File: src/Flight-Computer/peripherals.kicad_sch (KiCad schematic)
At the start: 32 parts, among them P10 Micro_SD_Card, P3 USB, P4 282837-6, Q1 QS5U17TR, Q2 QS5U17TR, U10 RFM95W-868S2, U3 CP2102-GMR(QFN28), U4 SST25VF040B-50-4I-S2AE-T, U5 TS391IYLT, U6 TS391IYLT, U7 TS391IYLT

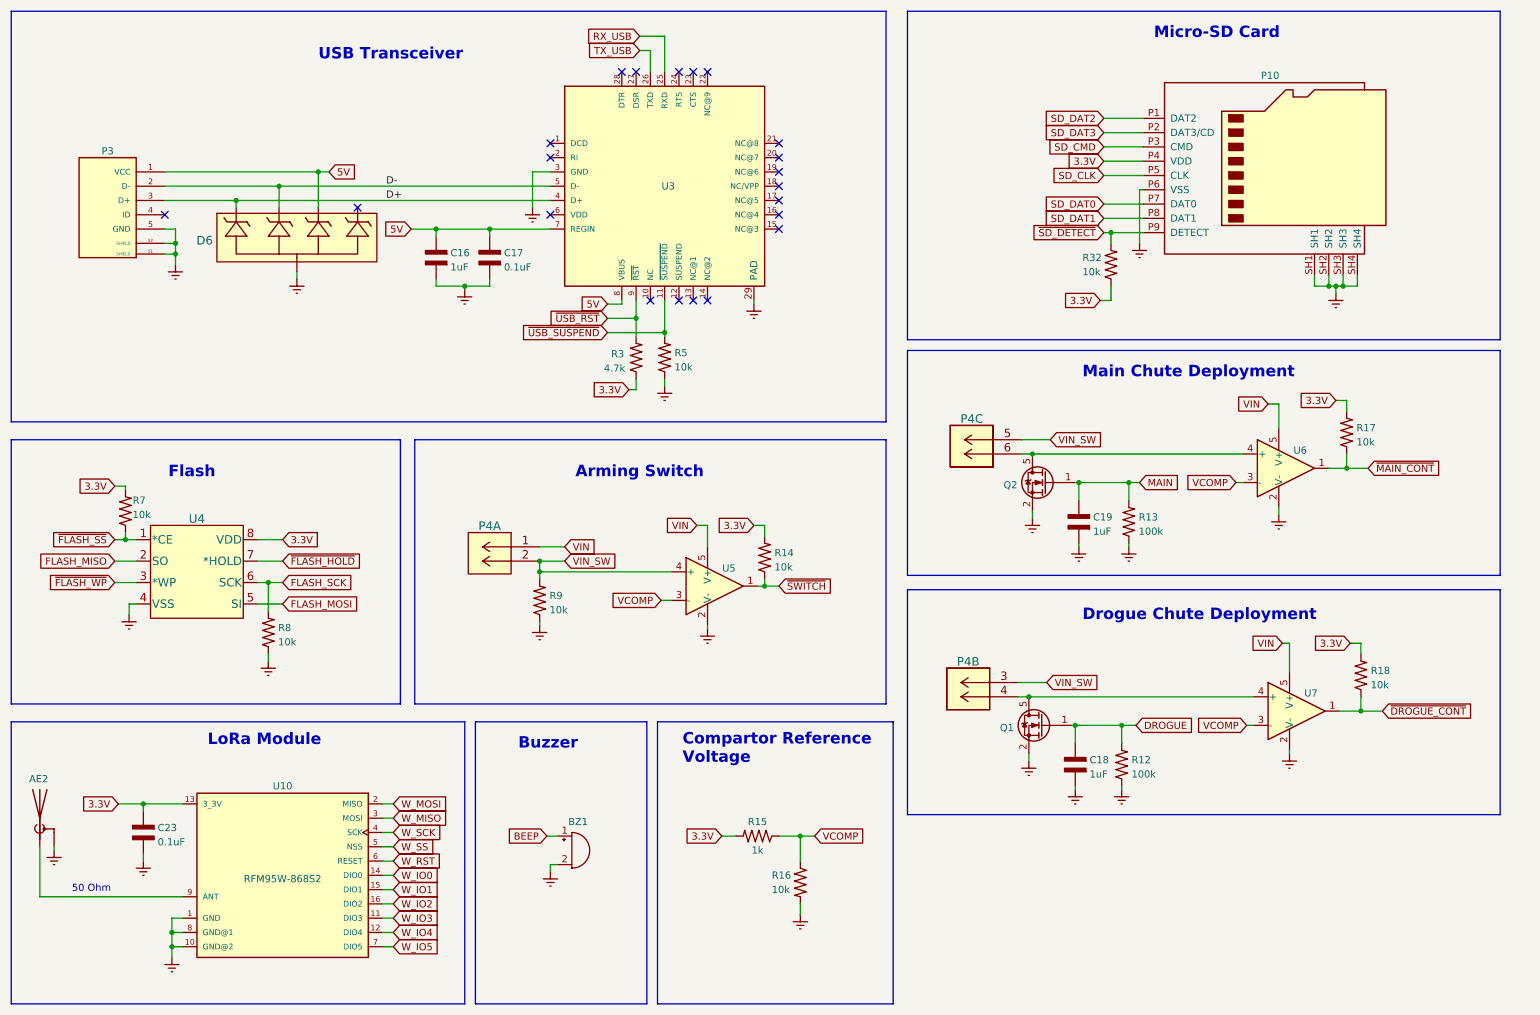
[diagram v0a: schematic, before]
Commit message: added usb detector to schemtaic
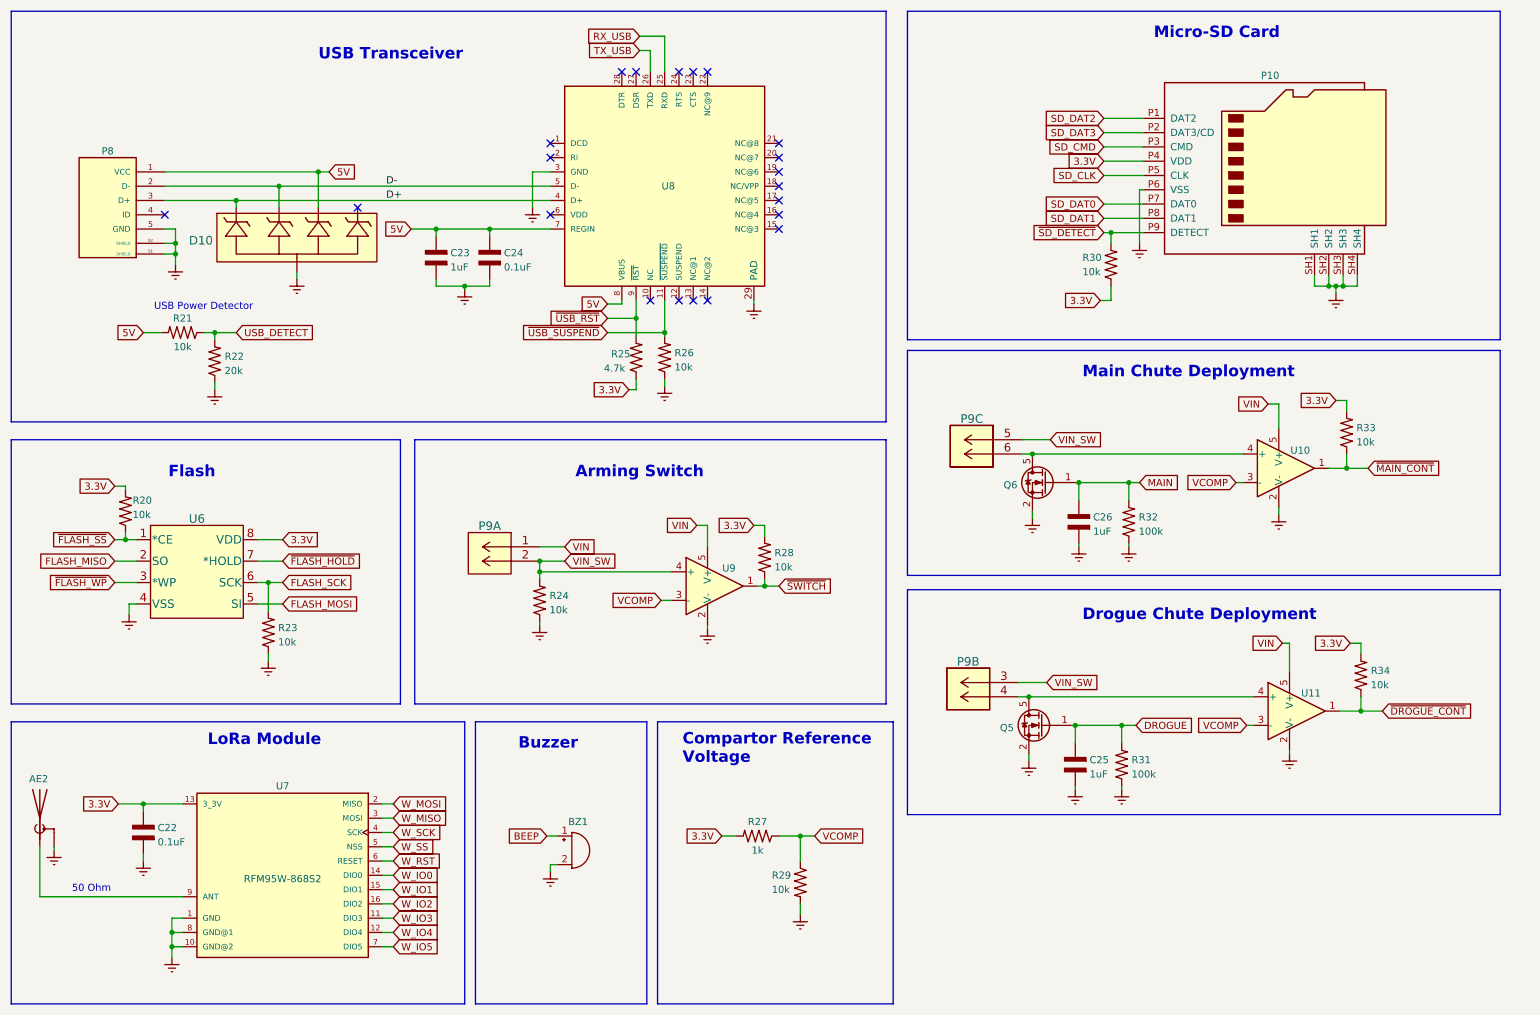
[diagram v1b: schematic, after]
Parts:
- added R21: 10k, Flight-Computer:RES_0603, symbol Flight-Computer:RES_0603
- added R22: 20k, Flight-Computer:RES_0603, symbol Flight-Computer:RES_0603
- renumbered C23 to C22, C16 to C23, C17 to C24, C18 to C25, C19 to C26, D6 to D10, P3 to P8, P4 to P9, Q1 to Q5, Q2 to Q6, R7 to R20, R8 to R23, R9 to R24, R3 to R25, R5 to R26, R15 to R27, R14 to R28, R16 to R29, R32 to R30, R12 to R31, R13 to R32, R17 to R33, R18 to R34, U6 to U10, U7 to U11, U4 to U6, U10 to U7, U3 to U8, U5 to U9
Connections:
- net 5V: now also R21.2
- net Earth: now also R22.1
- new net USB_DETECT: R21.1, R22.2
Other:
- note added: "USB Power Detector"

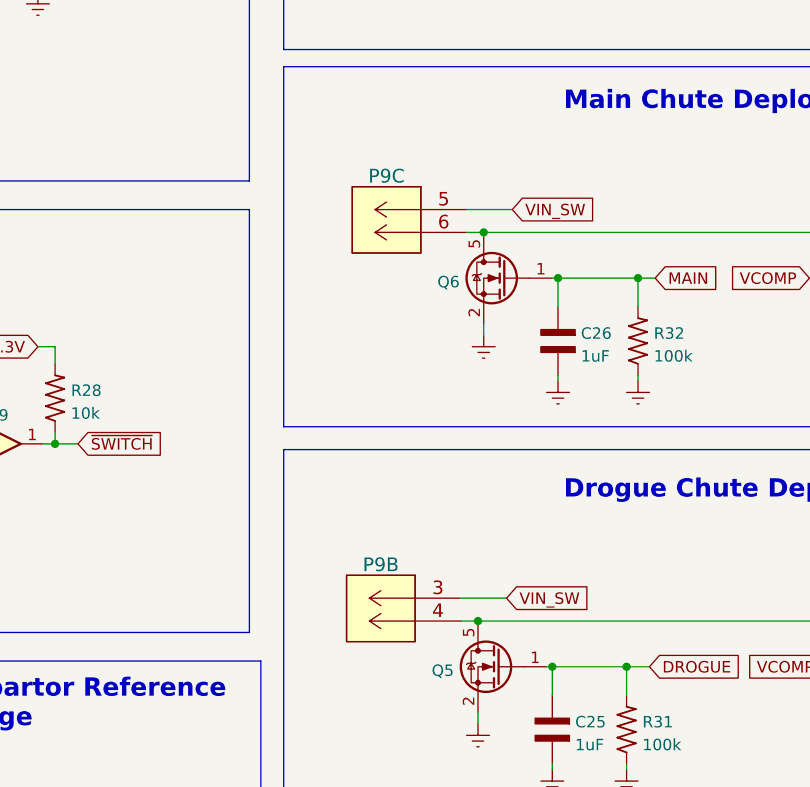
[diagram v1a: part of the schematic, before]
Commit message: replaced screw terminals with smaller parts
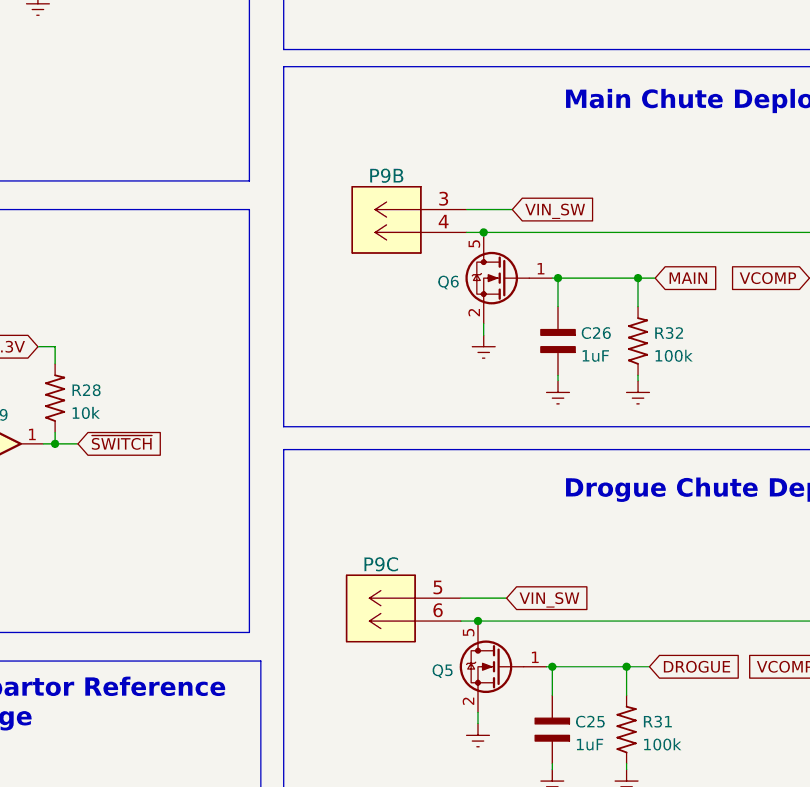
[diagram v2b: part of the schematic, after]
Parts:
- removed P9: 282837-6, Flight-Computer:282837-6, symbol Flight-Computer:282837-6
- added P9: 1984659, Flight-Computer:1984659, symbol Flight-Computer:1984659
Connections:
- net VIN: now also P9.1 (5)
- net VIN_SW: now also P9.2 (6), P9.3 (5), P9.5
- net at Q5.5 (D), U11.4 (+): now also P9.6
- net at Q6.5 (D), U10.4 (+): now also P9.4 (6)
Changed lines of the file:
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@@
   (junction (at 257.81 142.875) (diameter 0) (color 0 0 0 0)
   )
+  (junction (at 111.76 116.205) (diameter 0) (color 0 0 0 0)
+  )
   (junction (at 63.5 120.015) (diameter 0) (color 0 0 0 0)
   )
@@
   )
   (junction (at 41.275 159.385) (diameter 0) (color 0 0 0 0)
-  )
-  (junction (at 111.76 116.205) (diameter 0) (color 0 0 0 0)
   )
   (junction (at 254.635 67.31) (diameter 0) (color 0 0 0 0)
@@
     (pin "9")
   )
-  (symbol (lib_id "Flight-Computer:282837-6") (at 111.76 113.665 0) (mirror y) (unit 1)
-    (in_bom yes) (on_board yes) (fields_autoplaced)
-    (property "Reference" "P9" (id 0) (at 102.87 109.9581 0)
+  (symbol (lib_id "Flight-Computer:QS5U17TR") (at 201.295 145.415 0) (mirror y) (unit 1)
+    (in_bom yes) (on_board yes)
+    (property "Reference" "Q5" (id 0) (at 196.088 145.8488 0)
+      (effects (font (size 1.27 1.27)) (justify left))
+    )
+    (property "Value" "QS5U17TR" (id 1) (at 198.12 158.115 0)
+      (effects (font (size 1.27 1.27)) (justify left) hide)
+    )
+    (property "Footprint" "Engine-Controller:QS5U17TR" (id 2) (at 199.39 161.29 0)
+      (effects (font (size 1.27 1.27) italic) (justify left) hide)
+    )
+    (property "Datasheet" "https://www.onsemi.com/pub/Collateral/NDS7002A-D.PDF" (id 3) (at 202.565 164.465 0)
+      (effects (font (size 1.27 1.27)) (justify left) hide)
+    )
+    (pin "1")
+    (pin "2")
+    (pin "3")
+    (pin "4")
+    (pin "5")
+  )
+  (symbol (lib_id "Flight-Computer:1984659") (at 197.485 94.615 0) (mirror y) (unit 2)
+    (in_bom yes) (on_board yes) (fields_autoplaced)
+    (property "Reference" "P9" (id 0) (at 188.595 90.9081 0)
       (effects (font (size 1.524 1.524)))
     )
-    (property "Value" "282837-6" (id 1) (at 106.68 141.605 0)
+    (property "Value" "1984659" (id 1) (at 192.405 122.555 0)
       (effects (font (size 1.524 1.524)) hide)
     )
-    (property "Footprint" "Flight-Computer:282837-6" (id 2) (at 107.95 144.145 0)
+    (property "Footprint" "Flight-Computer:1984659" (id 2) (at 193.675 125.095 0)
       (effects (font (size 1.524 1.524)) hide)
     )
-    (property "Datasheet" "" (id 3) (at 111.76 113.665 0)
+    (property "Datasheet" "" (id 3) (at 197.485 94.615 0)
       (effects (font (size 1.524 1.524)) hide)
     )
@@
     (pin "5")
     (pin "6")
-  )
-  (symbol (lib_id "Flight-Computer:QS5U17TR") (at 201.295 145.415 0) (mirror y) (unit 1)
-    (in_bom yes) (on_board yes)
-    (property "Reference" "Q5" (id 0) (at 196.088 145.8488 0)
-      (effects (font (size 1.27 1.27)) (justify left))
-    )
-    (property "Value" "QS5U17TR" (id 1) (at 198.12 158.115 0)
-      (effects (font (size 1.27 1.27)) (justify left) hide)
-    )
-    (property "Footprint" "Engine-Controller:QS5U17TR" (id 2) (at 199.39 161.29 0)
-      (effects (font (size 1.27 1.27) italic) (justify left) hide)
-    )
-    (property "Datasheet" "https://www.onsemi.com/pub/Collateral/NDS7002A-D.PDF" (id 3) (at 202.565 164.465 0)
-      (effects (font (size 1.27 1.27)) (justify left) hide)
-    )
-    (pin "1")
-    (pin "2")
-    (pin "3")
-    (pin "4")
-    (pin "5")
   )
   (symbol (lib_id "Flight-Computer:TS391IYLT") (at 244.475 99.695 0) (unit 1)
@@
     (pin "2")
   )
-  (symbol (lib_id "Flight-Computer:Earth") (at 158.115 179.07 0) (unit 1)
-    (in_bom yes) (on_board yes) (fields_autoplaced)
-    (property "Reference" "#PWR050" (id 0) (at 158.115 185.42 0)
-      (effects (font (size 1.27 1.27)) hide)
-    )
-    (property "Value" "Earth" (id 1) (at 158.115 182.88 0)
-      (effects (font (size 1.27 1.27)) hide)
-    )
-    (property "Footprint" "" (id 2) (at 158.115 179.07 0)
-      (effects (font (size 1.27 1.27)) hide)
-    )
-    (property "Datasheet" "" (id 3) (at 158.115 179.07 0)
-      (effects (font (size 1.27 1.27)) hide)
-    )
-    (pin "1")
-  )
-  (symbol (lib_name "RES_0603_7") (lib_id "Flight-Computer:RES_0603") (at 255.27 93.345 90) (unit 1)
-    (in_bom yes) (on_board yes) (fields_autoplaced)
-    (property "Reference" "R33" (id 0) (at 257.0226 92.5103 90)
-      (effects (font (size 1.27 1.27)) (justify right))
-    )
-    (property "Value" "10k" (id 1) (at 257.0226 95.0472 90)
-      (effects (font (size 1.27 1.27)) (justify right))
-    )
-    (property "Footprint" "Flight-Computer:RES_0603" (id 2) (at 267.97 92.075 0)
-      (effects (font (size 1.27 1.27)) (justify left bottom) hide)
-    )
-    (property "Datasheet" "" (id 3) (at 255.27 93.345 0)
-      (effects (font (size 1.27 1.27)) (justify left bottom) hide)
-    )
-    (pin "1")
-    (pin "2")
-  )
-  (symbol (lib_id "Flight-Computer:Earth") (at 46.99 63.5 0) (unit 1)
-    (in_bom yes) (on_board yes) (fields_autoplaced)
-    (property "Reference" "#PWR039" (id 0) (at 46.99 69.85 0)
-      (effects (font (size 1.27 1.27)) hide)
-    )
-    (property "Value" "Earth" (id 1) (at 46.99 67.31 0)
-      (effects (font (size 1.27 1.27)) hide)
-    )
-    (property "Footprint" "" (id 2) (at 46.99 63.5 0)
-      (effects (font (size 1.27 1.27)) hide)
-    )
-    (property "Datasheet" "" (id 3) (at 46.99 63.5 0)
-      (effects (font (size 1.27 1.27)) hide)
-    )
-    (pin "1")
-  )
-  (symbol (lib_id "Flight-Computer:282837-6") (at 196.85 137.795 0) (mirror y) (unit 2)
+  (symbol (lib_id "Flight-Computer:1984659") (at 196.85 137.795 0) (mirror y) (unit 3)
     (in_bom yes) (on_board yes) (fields_autoplaced)
     (property "Reference" "P9" (id 0) (at 187.96 134.0881 0)
       (effects (font (size 1.524 1.524)))
     )
-    (property "Value" "282837-6" (id 1) (at 191.77 165.735 0)
+    (property "Value" "1984659" (id 1) (at 191.77 165.735 0)
       (effects (font (size 1.524 1.524)) hide)
     )
-    (property "Footprint" "Flight-Computer:282837-6" (id 2) (at 193.04 168.275 0)
+    (property "Footprint" "Flight-Computer:1984659" (id 2) (at 193.04 168.275 0)
       (effects (font (size 1.524 1.524)) hide)
     )
@@
     (pin "5")
     (pin "6")
+  )
+  (symbol (lib_id "Flight-Computer:Earth") (at 158.115 179.07 0) (unit 1)
+    (in_bom yes) (on_board yes) (fields_autoplaced)
+    (property "Reference" "#PWR050" (id 0) (at 158.115 185.42 0)
+      (effects (font (size 1.27 1.27)) hide)
+    )
+    (property "Value" "Earth" (id 1) (at 158.115 182.88 0)
+      (effects (font (size 1.27 1.27)) hide)
+    )
+    (property "Footprint" "" (id 2) (at 158.115 179.07 0)
+      (effects (font (size 1.27 1.27)) hide)
+    )
+    (property "Datasheet" "" (id 3) (at 158.115 179.07 0)
+      (effects (font (size 1.27 1.27)) hide)
+    )
+    (pin "1")
+  )
+  (symbol (lib_name "RES_0603_7") (lib_id "Flight-Computer:RES_0603") (at 255.27 93.345 90) (unit 1)
+    (in_bom yes) (on_board yes) (fields_autoplaced)
+    (property "Reference" "R33" (id 0) (at 257.0226 92.5103 90)
+      (effects (font (size 1.27 1.27)) (justify right))
+    )
+    (property "Value" "10k" (id 1) (at 257.0226 95.0472 90)
+      (effects (font (size 1.27 1.27)) (justify right))
+    )
+    (property "Footprint" "Flight-Computer:RES_0603" (id 2) (at 267.97 92.075 0)
+      (effects (font (size 1.27 1.27)) (justify left bottom) hide)
+    )
+    (property "Datasheet" "" (id 3) (at 255.27 93.345 0)
+      (effects (font (size 1.27 1.27)) (justify left bottom) hide)
+    )
+    (pin "1")
+    (pin "2")
+  )
+  (symbol (lib_id "Flight-Computer:Earth") (at 46.99 63.5 0) (unit 1)
+    (in_bom yes) (on_board yes) (fields_autoplaced)
+    (property "Reference" "#PWR039" (id 0) (at 46.99 69.85 0)
+      (effects (font (size 1.27 1.27)) hide)
+    )
+    (property "Value" "Earth" (id 1) (at 46.99 67.31 0)
+      (effects (font (size 1.27 1.27)) hide)
+    )
+    (property "Footprint" "" (id 2) (at 46.99 63.5 0)
+      (effects (font (size 1.27 1.27)) hide)
+    )
+    (property "Datasheet" "" (id 3) (at 46.99 63.5 0)
+      (effects (font (size 1.27 1.27)) hide)
+    )
+    (pin "1")
   )
   (symbol (lib_id "Flight-Computer:Micro_SD_Card") (at 241.935 45.085 0) (unit 1)
@@
     )
     (pin "1")
+  )
+  (symbol (lib_id "Flight-Computer:1984659") (at 111.76 113.665 0) (mirror y) (unit 1)
+    (in_bom yes) (on_board yes) (fields_autoplaced)
+    (property "Reference" "P9" (id 0) (at 102.87 109.9581 0)
+      (effects (font (size 1.524 1.524)))
+    )
+    (property "Value" "1984659" (id 1) (at 106.68 141.605 0)
+      (effects (font (size 1.524 1.524)) hide)
+    )
+    (property "Footprint" "Flight-Computer:1984659" (id 2) (at 107.95 144.145 0)
+      (effects (font (size 1.524 1.524)) hide)
+    )
+    (property "Datasheet" "" (id 3) (at 111.76 113.665 0)
+      (effects (font (size 1.524 1.524)) hide)
+    )
+    (pin "1")
+    (pin "2")
+    (pin "3")
+    (pin "4")
+    (pin "5")
+    (pin "6")
   )
   (symbol (lib_id "Flight-Computer:Earth") (at 199.39 108.585 0) (unit 1)
@@
     (pin "1")
   )
-  (symbol (lib_id "Flight-Computer:282837-6") (at 197.485 94.615 0) (mirror y) (unit 3)
-    (in_bom yes) (on_board yes) (fields_autoplaced)
-    (property "Reference" "P9" (id 0) (at 188.595 90.9081 0)
-      (effects (font (size 1.524 1.524)))
-    )
-    (property "Value" "282837-6" (id 1) (at 192.405 122.555 0)
-      (effects (font (size 1.524 1.524)) hide)
-    )
-    (property "Footprint" "Flight-Computer:282837-6" (id 2) (at 193.675 125.095 0)
-      (effects (font (size 1.524 1.524)) hide)
-    )
-    (property "Datasheet" "" (id 3) (at 197.485 94.615 0)
-      (effects (font (size 1.524 1.524)) hide)
-    )
-    (pin "1")
-    (pin "2")
-    (pin "3")
-    (pin "4")
-    (pin "5")
-    (pin "6")
-  )
   (symbol (lib_id "Flight-Computer:RES_0603") (at 213.36 63.5 90) (unit 1)

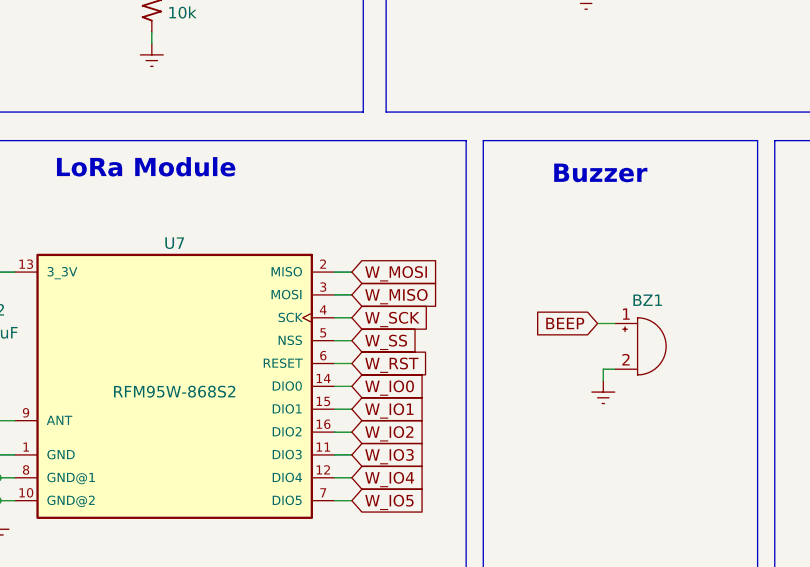
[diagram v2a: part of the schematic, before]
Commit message: fixed incorrect LoRa MISO and MOSI connections
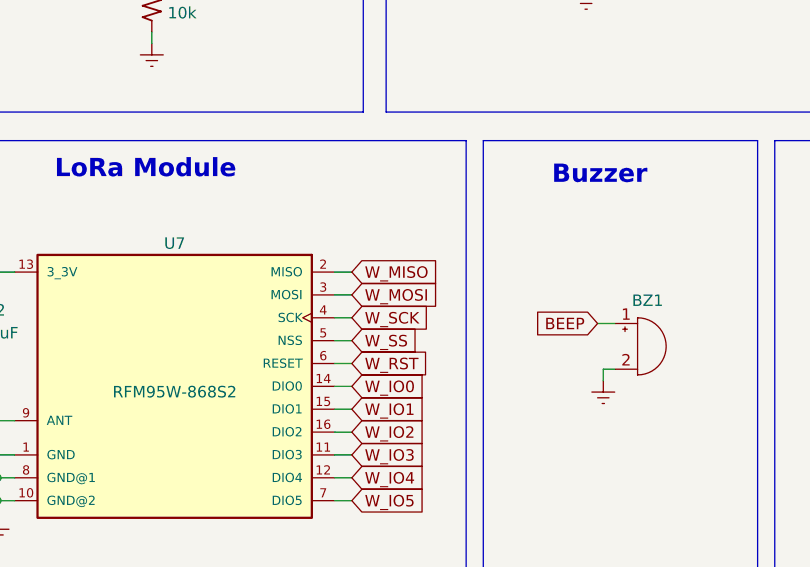
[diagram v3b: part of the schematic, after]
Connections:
- net W_MISO: now also U7.2 (MISO); no longer U7.3 (MOSI)
- net W_MOSI: now also U7.3 (MOSI); no longer U7.2 (MISO)

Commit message: matched footprints to symbols
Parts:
- Q5, Q6: footprint Engine-Controller:QS5U17TR -> Flight-Computer:QS5U17TR
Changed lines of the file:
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@@
       (effects (font (size 1.27 1.27)) (justify left) hide)
     )
-    (property "Footprint" "Engine-Controller:QS5U17TR" (id 2) (at 199.39 161.29 0)
+    (property "Footprint" "Flight-Computer:QS5U17TR" (id 2) (at 199.39 161.29 0)
       (effects (font (size 1.27 1.27) italic) (justify left) hide)
     )
@@
       (effects (font (size 1.27 1.27)) (justify left) hide)
     )
-    (property "Footprint" "Engine-Controller:QS5U17TR" (id 2) (at 200.025 118.11 0)
+    (property "Footprint" "Flight-Computer:QS5U17TR" (id 2) (at 200.025 118.11 0)
       (effects (font (size 1.27 1.27) italic) (justify left) hide)
     )
